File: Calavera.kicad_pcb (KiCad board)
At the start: 2 copper layers, 39.2 x 59.2 mm, 24 parts, among them Q1 Q_DUAL_NMOS, U1 AT42QT1012, U2 LMV932

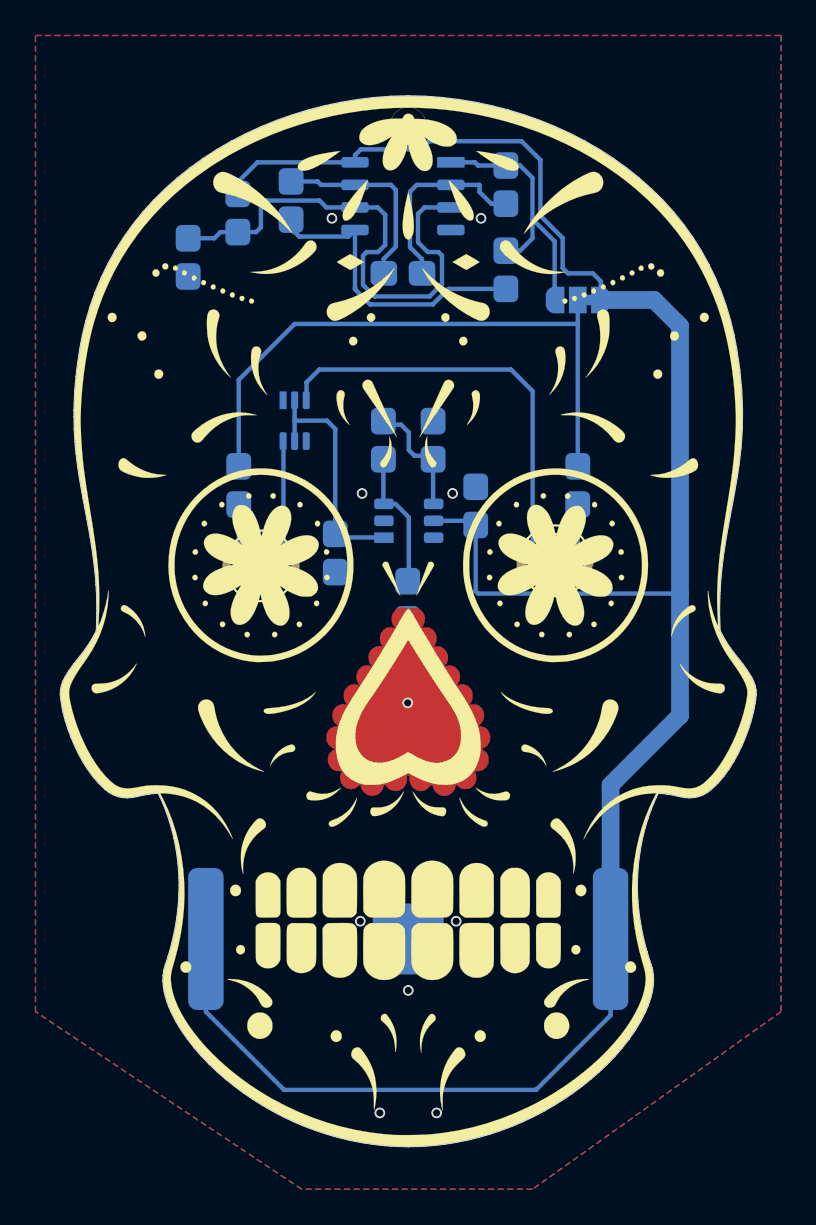
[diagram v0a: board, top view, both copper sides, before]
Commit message: Made tracks thicker, as they are easier to rip when overheat than I thought they would be
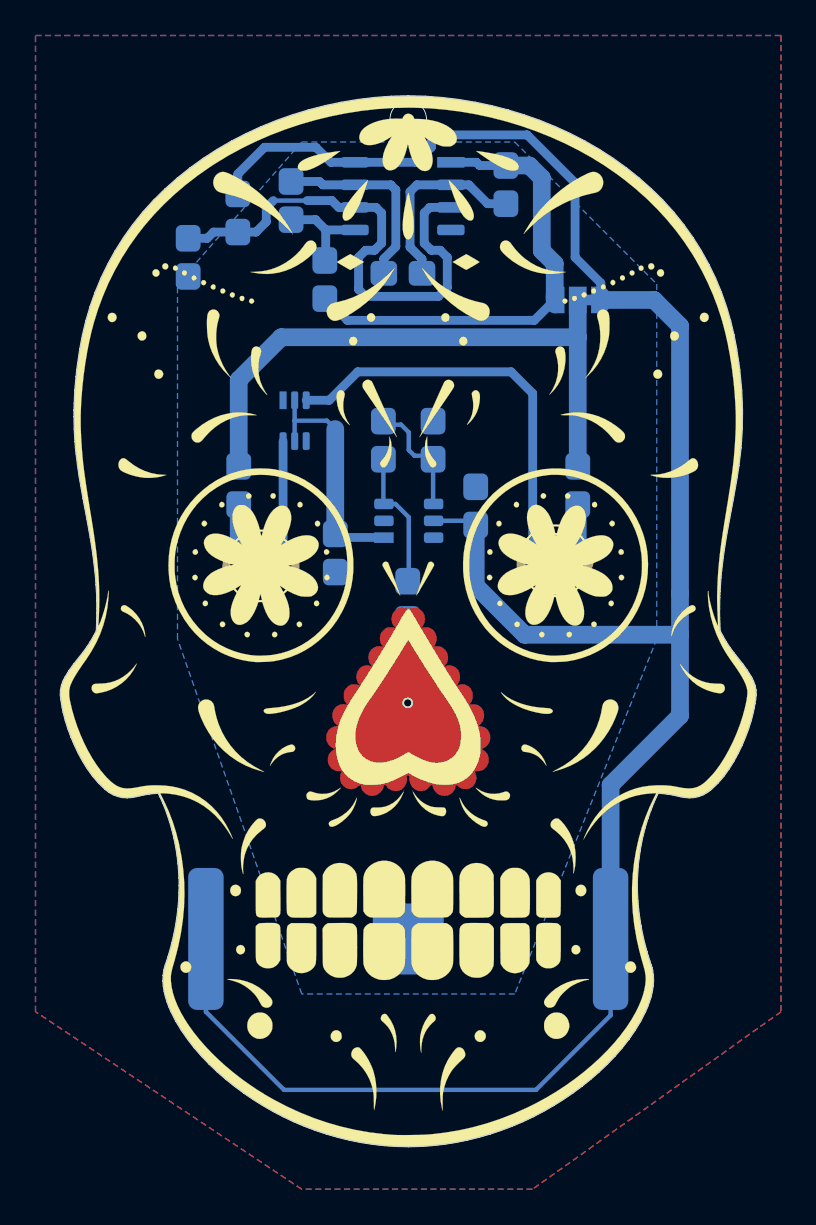
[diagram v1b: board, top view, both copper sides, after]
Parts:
- G3: footprint Calavera:Calavera_SolderMask_1200dpi_No_Border -> Calavera:Calavera_SolderMask_1200dpi_Border
- R9: value 2500 -> 2490
- moved R7 10.2 mm to (134.5, 83.5), turned to 90 degrees
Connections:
- net Net-(R7-Pad2) renamed VJ1
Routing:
- net VJ1: track 17.4 -> 5.56 mm
- net Vfade: track 14.9 -> 26.6 mm
- net VCC: track 123.3 -> 124.7 mm
- net VLEDK2: track 24.3 -> 23.4 mm
- net GND: vias 10 -> 0
- net (no net): vias 0 -> 1
- added copper zone on B.Cu, net (none)
- added copper zone on F.Cu, net (none)
- removed copper zone on F.Cu, net GND
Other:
- board text added: "DRC ERRORS ========= The two jumpers show an unconnected DRC error. That's a known issue with KiCad. It will have to stay like that for now IMPORT NETLIST =========== Importint the netlist shows two warnings for the copper plane. I wanted to leave them unconnected, so they will have to stay, I guess"

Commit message: Removed the Jumpers as they are not needed
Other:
- board text added: "IMPORT NETLIST =========== Importint the netlist shows two warnings for the copper plane. I wanted to leave them unconnected, so they will have to stay, I guess"
- board text removed: "DRC ERRORS ========= The two jumpers show an unconnected DRC error. That's a known issue with KiCad. It will have to stay like that for now IMPORT NETLIST =========== Importint the netlist shows two warnings for the copper plane. I wanted to leave them unconnected, so they will have to stay, I guess"
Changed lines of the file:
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@@
   )
   (setup
-    (last_trace_width 0.5)
+    (last_trace_width 0.25)
     (user_trace_width 0.16)
     (user_trace_width 0.2)
@@
       (xy 4.169635 0.319155) (xy 4.177933 0.307862) (xy 4.225172 0.248619) (xy 4.337225 0.383601)) (layer F.Mask) (width 0.01))
   )
-  (gr_text "DRC ERRORS\n=========\n\nThe two jumpers show an unconnected DRC error. That's a known issue\nwith KiCad. It will have to stay like that for now\n\nIMPORT NETLIST\n===========\n\nImportint the netlist shows two warnings for the copper\nplane. I wanted to leave them unconnected, so they \nwill have to stay, I guess" (at 162.8 78.7) (layer Dwgs.User)
+  (gr_text "IMPORT NETLIST\n===========\n\nImportint the netlist shows two warnings for the copper\nplane. I wanted to leave them unconnected, so they \nwill have to stay, I guess" (at 162.8 78.7) (layer Dwgs.User)
     (effects (font (size 0.5 0.5) (thickness 0.125)) (justify left))
   )
@@
   (segment (start 154.51 108.12) (end 154.51 103.56) (width 1) (layer B.Cu) (net 4))
   (segment (start 154.51 103.56) (end 154.51 101.24) (width 1) (layer B.Cu) (net 4))
-  (segment (start 143 97.375) (end 143 100.8) (width 1) (layer B.Cu) (net 4))
+  (segment (start 143 97.375) (end 143 100.8) (width 1) (layer B.Cu) (net 4) (status 10))
   (segment (start 145.76 103.56) (end 154.51 103.56) (width 1) (layer B.Cu) (net 4))
   (segment (start 143 100.8) (end 145.76 103.56) (width 1) (layer B.Cu) (net 4))
@@
   (segment (start 146.725 77.825) (end 146.725 81.925) (width 1) (layer B.Cu) (net 10))
   (segment (start 146.025 77.125) (end 146.725 77.825) (width 1) (layer B.Cu) (net 10))
-  (segment (start 146.3 85.85) (end 147.45 84.7) (width 0.5) (layer B.Cu) (net 10))
-  (segment (start 134.55 84.625) (end 135.775 85.85) (width 0.5) (layer B.Cu) (net 10))
+  (segment (start 146.3 85.85) (end 147.45 84.7) (width 0.5) (layer B.Cu) (net 10) (status 20))
+  (segment (start 134.55 84.625) (end 135.775 85.85) (width 0.5) (layer B.Cu) (net 10) (status 10))
   (segment (start 135.775 85.85) (end 146.3 85.85) (width 0.5) (layer B.Cu) (net 10))
   (via (at 139.17 107.4) (size 0.6) (drill 0.4) (layers F.Cu B.Cu) (net 11) (status 30))

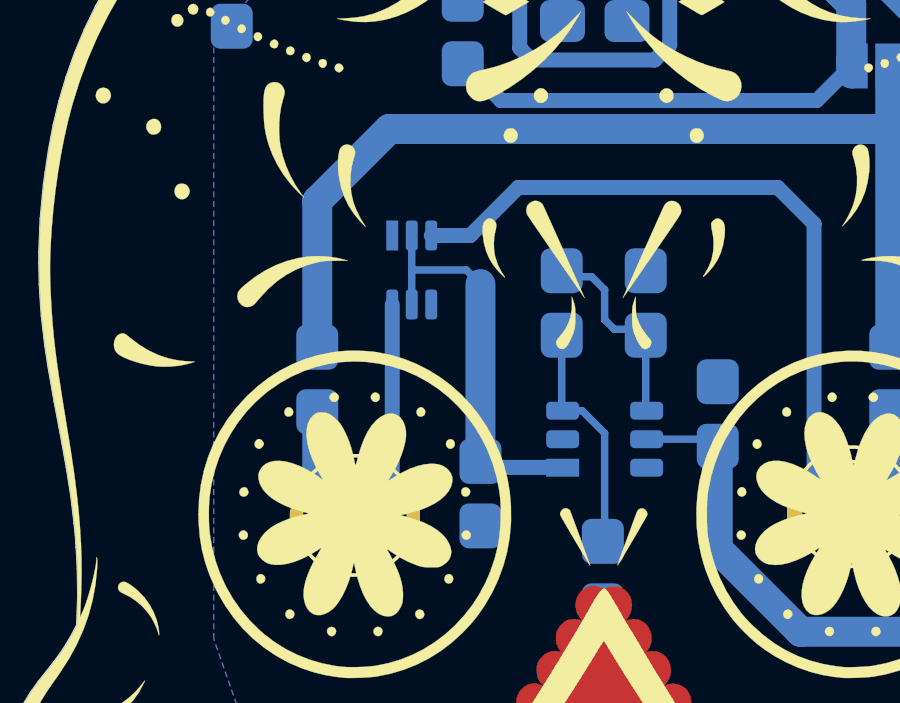
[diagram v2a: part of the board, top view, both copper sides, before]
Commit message: Changed the transistor footprint to a SOT23 as it was very tricky to solder.
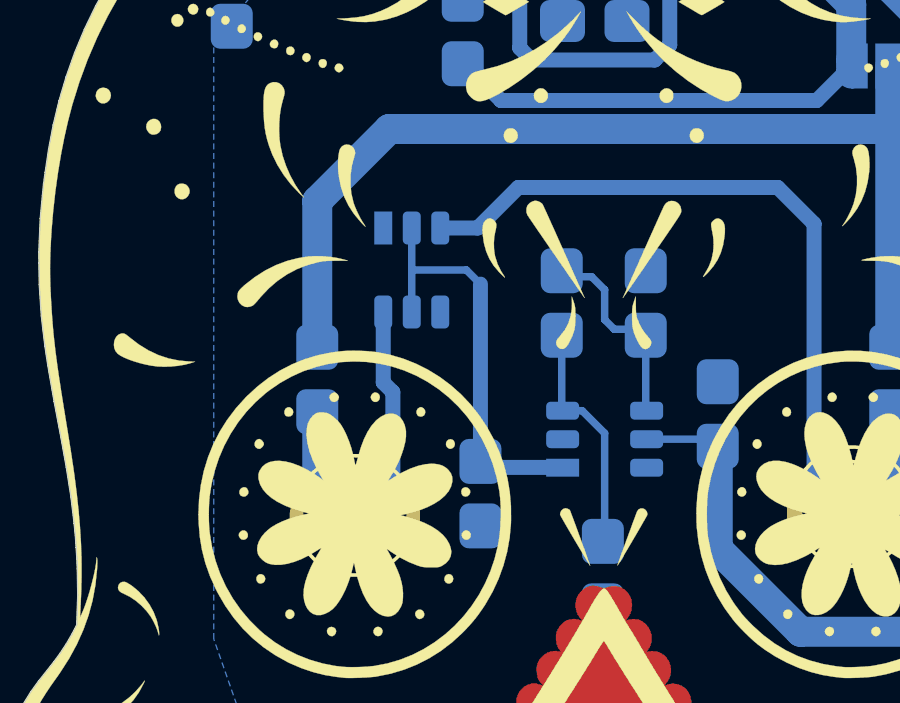
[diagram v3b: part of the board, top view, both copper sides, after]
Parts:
- Q1: footprint Calavera:SOT-363_NX138BKS_Handsolder -> Calavera:SOT23-6-NMOSx2_Handsolder

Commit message: Put everything on a single library, and the 3D models are now relative to the project path
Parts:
- C1, C2, C3: footprint felcana:0805-C_Handsolder -> Calavera:0805-C_Handsolder
- R1, R10, R2, R3, R4, R5, R6, R7, R8, R9: footprint felcana:0805-R_Handsolder -> Calavera:0805-R_Handsolder
